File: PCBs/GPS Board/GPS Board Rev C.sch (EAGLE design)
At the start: 4 parts

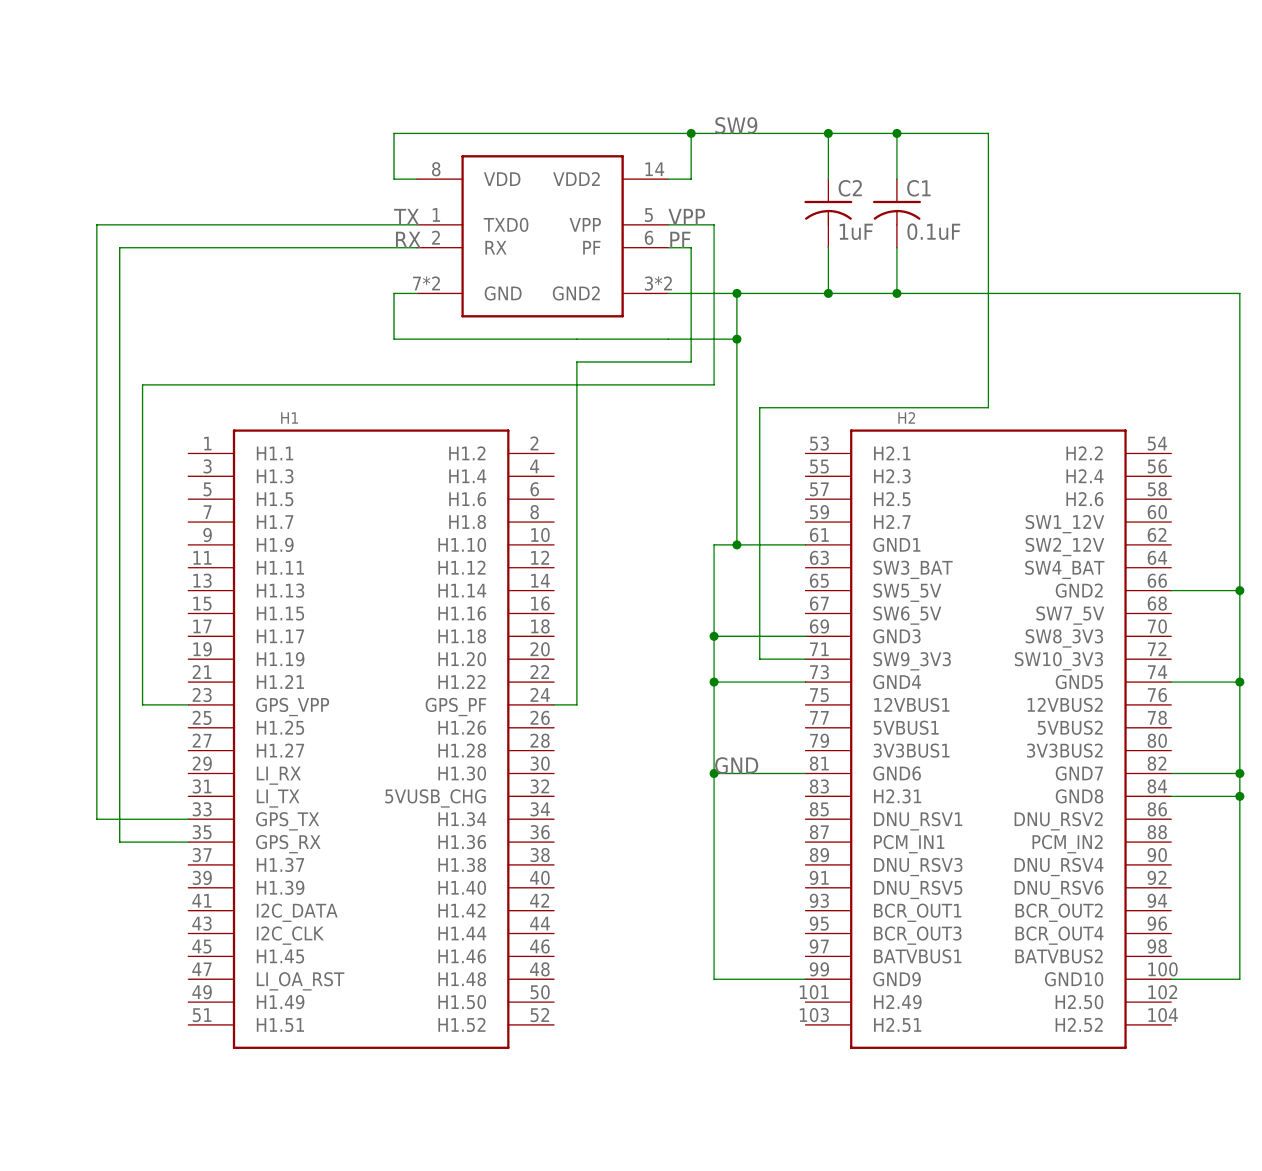
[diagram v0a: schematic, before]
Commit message: Add test pads
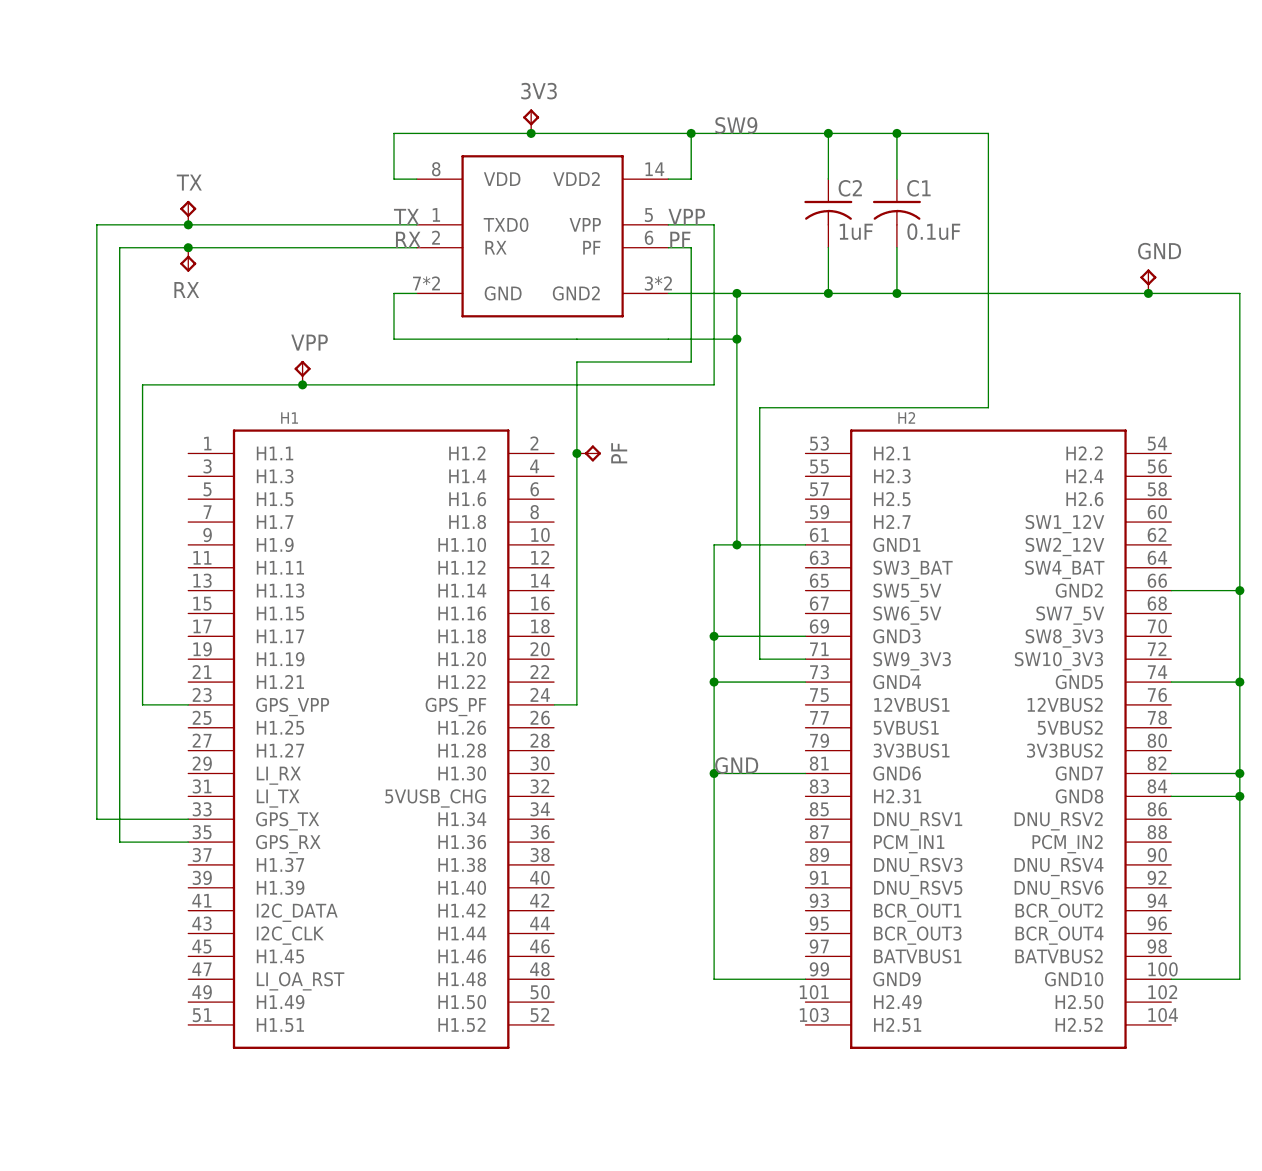
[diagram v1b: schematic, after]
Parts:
- added 3V3, GND, PF, RX, TX, VPP: TPTP10SQ, testpad:TPTP10SQ
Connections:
- net GND: now also GND.TP
- net PF: now also PF.TP
- net RX: now also RX.TP
- net SW9: now also 3V3.TP
- net TX: now also TX.TP
- net VPP: now also VPP.TP
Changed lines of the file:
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@@
 <part name="U$1" library="Cubesat" deviceset="PINAV-L1" device=""/>
 <part name="U$2" library="Cubesat" deviceset="PC104_NO_DIMENSION" device=""/>
+<part name="GND" library="testpad" library_urn="urn:adsk.eagle:library:385" deviceset="TP" device="TP10SQ" package3d_urn="urn:adsk.eagle:package:27962/1"/>
+<part name="TX" library="testpad" library_urn="urn:adsk.eagle:library:385" deviceset="TP" device="TP10SQ" package3d_urn="urn:adsk.eagle:package:27962/1"/>
+<part name="RX" library="testpad" library_urn="urn:adsk.eagle:library:385" deviceset="TP" device="TP10SQ" package3d_urn="urn:adsk.eagle:package:27962/1"/>
+<part name="3V3" library="testpad" library_urn="urn:adsk.eagle:library:385" deviceset="TP" device="TP10SQ" package3d_urn="urn:adsk.eagle:package:27962/1"/>
+<part name="VPP" library="testpad" library_urn="urn:adsk.eagle:library:385" deviceset="TP" device="TP10SQ" package3d_urn="urn:adsk.eagle:package:27962/1"/>
+<part name="PF" library="testpad" library_urn="urn:adsk.eagle:library:385" deviceset="TP" device="TP10SQ" package3d_urn="urn:adsk.eagle:package:27962/1"/>
 </parts>
 <sheets>
@@
 <instance part="U$1" gate="G$1" x="33.02" y="76.2"/>
 <instance part="U$2" gate="A" x="-7.62" y="58.42"/>
+<instance part="GND" gate="G$1" x="99.06" y="78.74"/>
+<instance part="TX" gate="G$1" x="-7.62" y="86.36"/>
+<instance part="RX" gate="G$1" x="-7.62" y="78.74" rot="R180"/>
+<instance part="3V3" gate="G$1" x="30.48" y="96.52"/>
+<instance part="VPP" gate="G$1" x="5.08" y="68.58"/>
+<instance part="PF" gate="G$1" x="38.1" y="58.42" rot="R270"/>
 </instances>
 <busses>
@@
 <junction x="71.12" y="93.98"/>
 <label x="50.8" y="93.98" size="1.778" layer="95"/>
-<wire x1="48.26" y1="93.98" x2="15.24" y2="93.98" width="0.1524" layer="91"/>
+<wire x1="48.26" y1="93.98" x2="30.48" y2="93.98" width="0.1524" layer="91"/>
+<wire x1="30.48" y1="93.98" x2="15.24" y2="93.98" width="0.1524" layer="91"/>
 <wire x1="15.24" y1="93.98" x2="15.24" y2="88.9" width="0.1524" layer="91"/>
 <junction x="48.26" y="93.98"/>
@@
 <pinref part="U$1" gate="G$1" pin="VDD2"/>
 <pinref part="U$2" gate="A" pin="SW9_3V3"/>
+<pinref part="3V3" gate="G$1" pin="TP"/>
+<junction x="30.48" y="93.98"/>
 </segment>
 </net>
@@
 <wire x1="71.12" y1="81.28" x2="71.12" y2="76.2" width="0.1524" layer="91"/>
 <junction x="71.12" y="76.2"/>
-<wire x1="71.12" y1="76.2" x2="109.22" y2="76.2" width="0.1524" layer="91"/>
+<wire x1="71.12" y1="76.2" x2="99.06" y2="76.2" width="0.1524" layer="91"/>
+<wire x1="99.06" y1="76.2" x2="109.22" y2="76.2" width="0.1524" layer="91"/>
 <wire x1="109.22" y1="76.2" x2="109.22" y2="43.18" width="0.1524" layer="91"/>
 <wire x1="101.6" y1="43.18" x2="109.22" y2="43.18" width="0.1524" layer="91"/>
@@
 <pinref part="U$2" gate="A" pin="GND9"/>
 <pinref part="U$2" gate="A" pin="GND10"/>
+<pinref part="GND" gate="G$1" pin="TP"/>
+<junction x="99.06" y="76.2"/>
 </segment>
 </net>
@@
 <wire x1="45.72" y1="83.82" x2="50.8" y2="83.82" width="0.1524" layer="91"/>
 <wire x1="50.8" y1="83.82" x2="50.8" y2="66.04" width="0.1524" layer="91"/>
-<wire x1="50.8" y1="66.04" x2="-12.7" y2="66.04" width="0.1524" layer="91"/>
+<wire x1="50.8" y1="66.04" x2="5.08" y2="66.04" width="0.1524" layer="91"/>
+<wire x1="5.08" y1="66.04" x2="-12.7" y2="66.04" width="0.1524" layer="91"/>
 <wire x1="-12.7" y1="66.04" x2="-12.7" y2="30.48" width="0.1524" layer="91"/>
 <wire x1="-12.7" y1="30.48" x2="-7.62" y2="30.48" width="0.1524" layer="91"/>
@@
 <pinref part="U$1" gate="G$1" pin="VPP"/>
 <pinref part="U$2" gate="A" pin="GPS_VPP"/>
+<pinref part="VPP" gate="G$1" pin="TP"/>
+<junction x="5.08" y="66.04"/>
 </segment>
 </net>
@@
 <wire x1="48.26" y1="81.28" x2="48.26" y2="68.58" width="0.1524" layer="91"/>
 <wire x1="48.26" y1="68.58" x2="35.56" y2="68.58" width="0.1524" layer="91"/>
-<wire x1="35.56" y1="68.58" x2="35.56" y2="30.48" width="0.1524" layer="91"/>
+<wire x1="35.56" y1="68.58" x2="35.56" y2="58.42" width="0.1524" layer="91"/>
+<wire x1="35.56" y1="58.42" x2="35.56" y2="30.48" width="0.1524" layer="91"/>
 <wire x1="35.56" y1="30.48" x2="33.02" y2="30.48" width="0.1524" layer="91"/>
 <label x="45.72" y="81.28" size="1.778" layer="95"/>
 <pinref part="U$1" gate="G$1" pin="PF"/>
 <pinref part="U$2" gate="A" pin="GPS_PF"/>
+<pinref part="PF" gate="G$1" pin="TP"/>
+<junction x="35.56" y="58.42"/>
 </segment>
 </net>
 <net name="TX" class="0">
 <segment>
-<wire x1="17.78" y1="83.82" x2="-17.78" y2="83.82" width="0.1524" layer="91"/>
+<wire x1="17.78" y1="83.82" x2="-7.62" y2="83.82" width="0.1524" layer="91"/>
+<wire x1="-7.62" y1="83.82" x2="-17.78" y2="83.82" width="0.1524" layer="91"/>
 <wire x1="-17.78" y1="83.82" x2="-17.78" y2="17.78" width="0.1524" layer="91"/>
 <wire x1="-17.78" y1="17.78" x2="-7.62" y2="17.78" width="0.1524" layer="91"/>
@@
 <pinref part="U$1" gate="G$1" pin="TXD0"/>
 <pinref part="U$2" gate="A" pin="GPS_TX"/>
+<pinref part="TX" gate="G$1" pin="TP"/>
+<junction x="-7.62" y="83.82"/>
 </segment>
 </net>
 <net name="RX" class="0">
 <segment>
-<wire x1="17.78" y1="81.28" x2="-15.24" y2="81.28" width="0.1524" layer="91"/>
+<wire x1="17.78" y1="81.28" x2="-7.62" y2="81.28" width="0.1524" layer="91"/>
+<wire x1="-7.62" y1="81.28" x2="-15.24" y2="81.28" width="0.1524" layer="91"/>
 <wire x1="-15.24" y1="81.28" x2="-15.24" y2="15.24" width="0.1524" layer="91"/>
 <wire x1="-15.24" y1="15.24" x2="-7.62" y2="15.24" width="0.1524" layer="91"/>
@@
 <pinref part="U$1" gate="G$1" pin="RX"/>
 <pinref part="U$2" gate="A" pin="GPS_RX"/>
+<pinref part="RX" gate="G$1" pin="TP"/>
+<junction x="-7.62" y="81.28"/>
 </segment>
 </net>

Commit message: So. many. changes.
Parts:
- removed U$1: PINAV-L1, Cubesat:PINAV-L1
- added PINAV-CONNECTOR: HLE-110-02-X-DV-BE-A, HLE-110-02-X-DV-BE-A:HLE-110-02-X-DV-BE-A
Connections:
- net GND: now also PINAV-CONNECTOR.15, PINAV-CONNECTOR.7; no longer U$1.GND, U$1.GND2
- net PF: now also PINAV-CONNECTOR.6; no longer U$1.PF
- net RX: now also PINAV-CONNECTOR.2; no longer U$1.RX
- net SW9: now also PINAV-CONNECTOR.14, PINAV-CONNECTOR.8; no longer U$1.VDD, U$1.VDD2
- net TX: now also PINAV-CONNECTOR.1; no longer U$1.TXD0
- net VPP: now also PINAV-CONNECTOR.5; no longer U$1.VPP
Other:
- moved on the sheet: 3V3, C1, C2, GND, PF, RX, TX, VPP

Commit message: Update piNAV connector to PE-BE model
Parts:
- PINAV-CONNECTOR: value HLE-110-02-X-DV-BE-A -> HLE-110-02-X-DVHLE-110-X-DV-PE-BA; device HLE-110-02-X-DV-BE-A:HLE-110-02-X-DV-BE-A -> HLE-110-02-X-DV:HLE-110-02-X-DVHLE-110-X-DV-PE-BA
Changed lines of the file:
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@@
 <grid distance="0.1" unitdist="inch" unit="inch" style="lines" multiple="1" display="no" altdistance="0.01" altunitdist="inch" altunit="inch"/>
 <layers>
-<layer number="1" name="Top" color="4" fill="1" visible="no" active="no"/>
-<layer number="2" name="Route2" color="1" fill="3" visible="no" active="no"/>
-<layer number="3" name="Route3" color="4" fill="3" visible="no" active="no"/>
-<layer number="4" name="Route4" color="1" fill="4" visible="no" active="no"/>
-<layer number="5" name="Route5" color="4" fill="4" visible="no" active="no"/>
-<layer number="6" name="Route6" color="1" fill="8" visible="no" active="no"/>
-<layer number="7" name="Route7" color="4" fill="8" visible="no" active="no"/>
-<layer number="8" name="Route8" color="1" fill="2" visible="no" active="no"/>
-<layer number="9" name="Route9" color="4" fill="2" visible="no" active="no"/>
-<layer number="10" name="Route10" color="1" fill="7" visible="no" active="no"/>
-<layer number="11" name="Route11" color="4" fill="7" visible="no" active="no"/>
-<layer number="12" name="Route12" color="1" fill="5" visible="no" active="no"/>
-<layer number="13" name="Route13" color="4" fill="5" visible="no" active="no"/>
-<layer number="14" name="Route14" color="1" fill="6" visible="no" active="no"/>
-<layer number="15" name="Route15" color="4" fill="6" visible="no" active="no"/>
-<layer number="16" name="Bottom" color="1" fill="1" visible="no" active="no"/>
-<layer number="17" name="Pads" color="2" fill="1" visible="no" active="no"/>
-<layer number="18" name="Vias" color="2" fill="1" visible="no" active="no"/>
-<layer number="19" name="Unrouted" color="6" fill="1" visible="no" active="no"/>
-<layer number="20" name="Dimension" color="24" fill="1" visible="no" active="no"/>
-<layer number="21" name="tPlace" color="7" fill="1" visible="no" active="no"/>
-<layer number="22" name="bPlace" color="7" fill="1" visible="no" active="no"/>
-<layer number="23" name="tOrigins" color="15" fill="1" visible="no" active="no"/>
-<layer number="24" name="bOrigins" color="15" fill="1" visible="no" active="no"/>
-<layer number="25" name="tNames" color="7" fill="1" visible="no" active="no"/>
-<layer number="26" name="bNames" color="7" fill="1" visible="no" active="no"/>
-<layer number="27" name="tValues" color="7" fill="1" visible="no" active="no"/>
-<layer number="28" name="bValues" color="7" fill="1" visible="no" active="no"/>
+<layer number="1" name="Top" color="4" fill="1" visible="yes" active="no"/>
+<layer number="2" name="Route2" color="1" fill="3" visible="yes" active="no"/>
+<layer number="3" name="Route3" color="4" fill="3" visible="yes" active="no"/>
+<layer number="4" name="Route4" color="1" fill="4" visible="yes" active="no"/>
+<layer number="5" name="Route5" color="4" fill="4" visible="yes" active="no"/>
+<layer number="6" name="Route6" color="1" fill="8" visible="yes" active="no"/>
+<layer number="7" name="Route7" color="4" fill="8" visible="yes" active="no"/>
+<layer number="8" name="Route8" color="1" fill="2" visible="yes" active="no"/>
+<layer number="9" name="Route9" color="4" fill="2" visible="yes" active="no"/>
+<layer number="10" name="Route10" color="1" fill="7" visible="yes" active="no"/>
+<layer number="11" name="Route11" color="4" fill="7" visible="yes" active="no"/>
+<layer number="12" name="Route12" color="1" fill="5" visible="yes" active="no"/>
+<layer number="13" name="Route13" color="4" fill="5" visible="yes" active="no"/>
+<layer number="14" name="Route14" color="1" fill="6" visible="yes" active="no"/>
+<layer number="15" name="Route15" color="4" fill="6" visible="yes" active="no"/>
+<layer number="16" name="Bottom" color="1" fill="1" visible="yes" active="no"/>
+<layer number="17" name="Pads" color="2" fill="1" visible="yes" active="no"/>
+<layer number="18" name="Vias" color="2" fill="1" visible="yes" active="no"/>
+<layer number="19" name="Unrouted" color="6" fill="1" visible="yes" active="no"/>
+<layer number="20" name="Dimension" color="24" fill="1" visible="yes" active="no"/>
+<layer number="21" name="tPlace" color="7" fill="1" visible="yes" active="no"/>
+<layer number="22" name="bPlace" color="7" fill="1" visible="yes" active="no"/>
+<layer number="23" name="tOrigins" color="15" fill="1" visible="yes" active="no"/>
+<layer number="24" name="bOrigins" color="15" fill="1" visible="yes" active="no"/>
+<layer number="25" name="tNames" color="7" fill="1" visible="yes" active="no"/>
+<layer number="26" name="bNames" color="7" fill="1" visible="yes" active="no"/>
+<layer number="27" name="tValues" color="7" fill="1" visible="yes" active="no"/>
+<layer number="28" name="bValues" color="7" fill="1" visible="yes" active="no"/>
 <layer number="29" name="tStop" color="7" fill="3" visible="no" active="no"/>
 <layer number="30" name="bStop" color="7" fill="6" visible="no" active="no"/>
@@
 <layer number="35" name="tGlue" color="7" fill="4" visible="no" active="no"/>
 <layer number="36" name="bGlue" color="7" fill="5" visible="no" active="no"/>
-<layer number="37" name="tTest" color="7" fill="1" visible="no" active="no"/>
-<layer number="38" name="bTest" color="7" fill="1" visible="no" active="no"/>
+<layer number="37" name="tTest" color="7" fill="1" visible="yes" active="no"/>
+<layer number="38" name="bTest" color="7" fill="1" visible="yes" active="no"/>
 <layer number="39" name="tKeepout" color="4" fill="11" visible="no" active="no"/>
 <layer number="40" name="bKeepout" color="1" fill="11" visible="no" active="no"/>
@@
 <layer number="44" name="Drills" color="7" fill="1" visible="no" active="no"/>
 <layer number="45" name="Holes" color="7" fill="1" visible="no" active="no"/>
-<layer number="46" name="Milling" color="3" fill="1" visible="no" active="no"/>
-<layer number="47" name="Measures" color="7" fill="1" visible="no" active="no"/>
-<layer number="48" name="Document" color="7" fill="1" visible="no" active="no"/>
-<layer number="49" name="Reference" color="7" fill="1" visible="no" active="no"/>
-<layer number="50" name="dxf" color="7" fill="1" visible="no" active="no"/>
-<layer number="51" name="tDocu" color="7" fill="1" visible="no" active="no"/>
-<layer number="52" name="bDocu" color="7" fill="1" visible="no" active="no"/>
-<layer number="53" name="tGND_GNDA" color="7" fill="9" visible="no" active="no"/>
-<layer number="54" name="bGND_GNDA" color="1" fill="9" visible="no" active="no"/>
-<layer number="56" name="wert" color="7" fill="1" visible="no" active="no"/>
-<layer number="57" name="tCAD" color="7" fill="1" visible="no" active="no"/>
-<layer number="58" name="bCAD" color="7" fill="1" visible="no" active="no"/>
+<layer number="46" name="Milling" color="3" fill="1" visible="yes" active="no"/>
+<layer number="47" name="Measures" color="7" fill="1" visible="yes" active="no"/>
+<layer number="48" name="Document" color="7" fill="1" visible="yes" active="no"/>
+<layer number="49" name="Reference" color="7" fill="1" visible="yes" active="no"/>
+<layer number="50" name="dxf" color="7" fill="1" visible="yes" active="no"/>
+<layer number="51" name="tDocu" color="7" fill="1" visible="yes" active="no"/>
+<layer number="52" name="bDocu" color="7" fill="1" visible="yes" active="no"/>
+<layer number="53" name="tGND_GNDA" color="7" fill="9" visible="yes" active="no"/>
+<layer number="54" name="bGND_GNDA" color="1" fill="9" visible="yes" active="no"/>
+<layer number="56" name="wert" color="7" fill="1" visible="yes" active="no"/>
+<layer number="57" name="tCAD" color="7" fill="1" visible="yes" active="no"/>
+<layer number="58" name="bCAD" color="7" fill="1" visible="yes" active="no"/>
 <layer number="88" name="SimResults" color="9" fill="1" visible="yes" active="yes"/>
 <layer number="89" name="SimProbes" color="9" fill="1" visible="yes" active="yes"/>
@@
 <part name="VPP" library="testpad" library_urn="urn:adsk.eagle:library:385" deviceset="TP" device="TP10SQ" package3d_urn="urn:adsk.eagle:package:27962/1"/>
 <part name="PF" library="testpad" library_urn="urn:adsk.eagle:library:385" deviceset="TP" device="TP10SQ" package3d_urn="urn:adsk.eagle:package:27962/1"/>
-<part name="PINAV-CONNECTOR" library="HLE-110-02-X-DV-BE-A" deviceset="HLE-110-02-X-DV-BE-A" device=""/>
+<part name="PINAV-CONNECTOR" library="HLE-110-02-X-DV" deviceset="HLE-110-02-X-DV" device="HLE-110-X-DV-PE-BA"/>
 </parts>
 <sheets>
